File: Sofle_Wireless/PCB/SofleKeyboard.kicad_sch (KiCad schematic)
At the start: 139 parts, among them J1 Conn_01x05, J2 Conn_01x02, SW1 SW1, SW10 SW10, SW11 SW11, SW12 SW12, SW13 SW13, SW14 SW14, SW15 SW15, SW16 SW16, SW17 SW17, SW18 SW18, SW19 SW19, SW2 SW2, SW20 SW20, SW21 SW21, SW22 SW22, SW23 SW23, SW24 SW24, SW25 SW19, SW26 SW26, SW27 SW27, SW28 SW28, SW29 SW29, SW3 SW3, SW30 SW30, SW4 SW4, SW5 SW5, SW6 SW6, SW7 SW7, SW8 SW8, SW9 SW9, U1 NICE!NANO

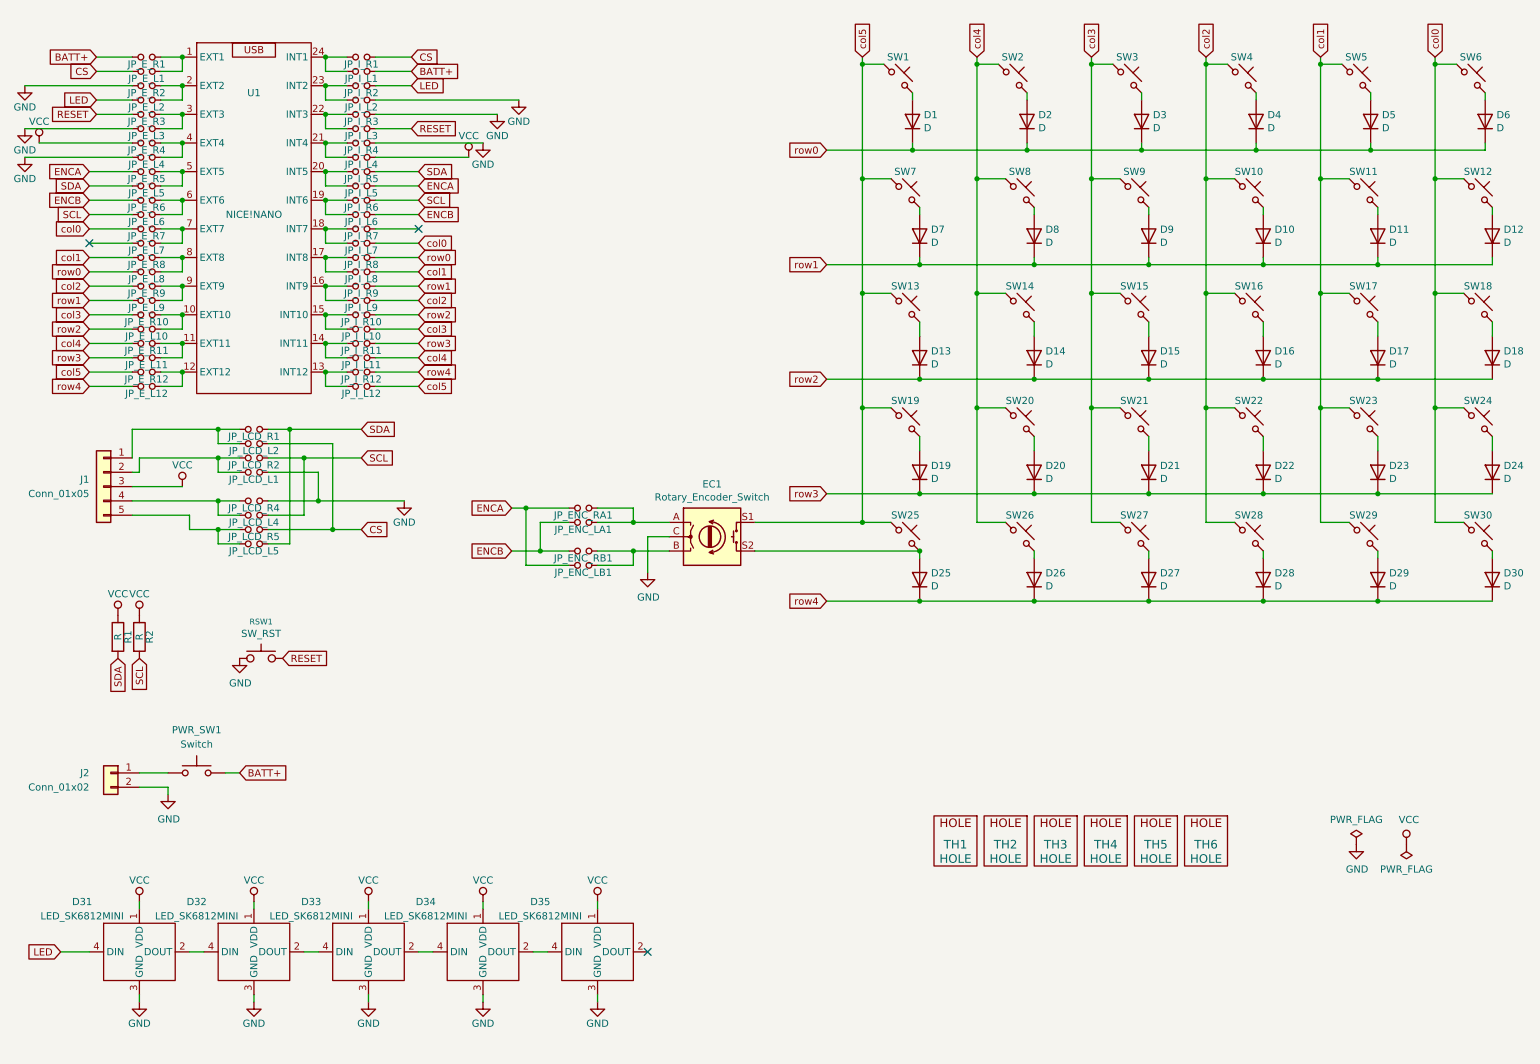
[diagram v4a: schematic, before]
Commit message: Exploration of multiple sheet for Schematic
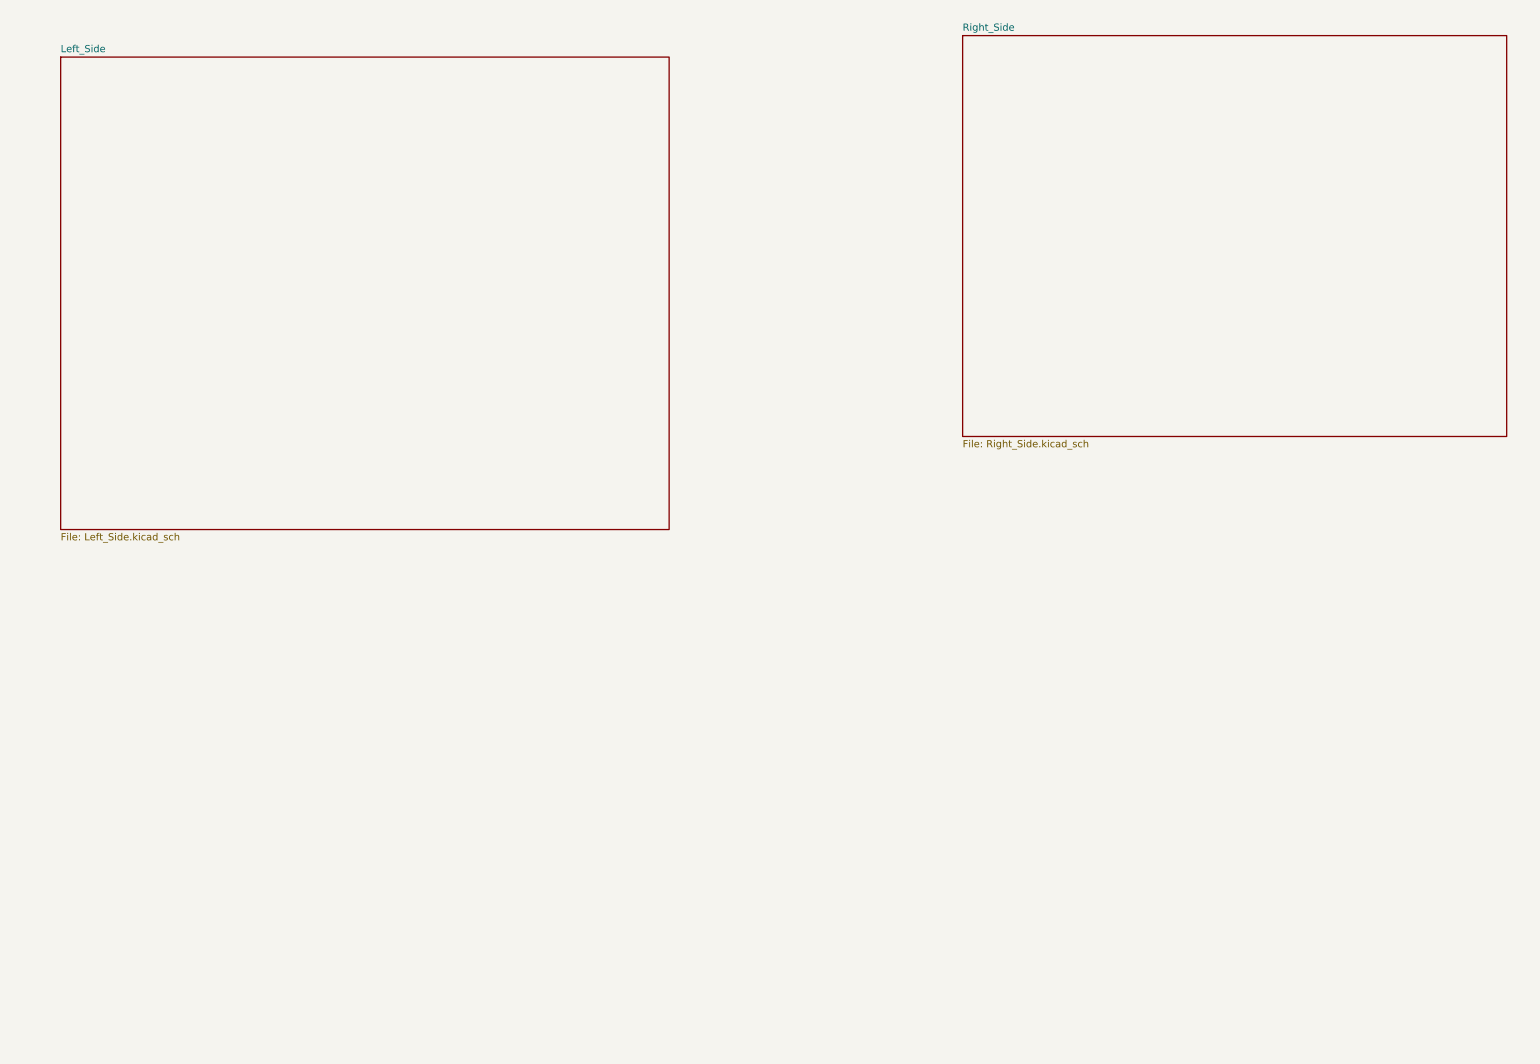
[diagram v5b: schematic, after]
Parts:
- removed D1, D10, D11, D12, D13, D14, D15, D16, D17, D18, D19, D2, D20, D21, D22, D23, D24, D25, D26, D27, D28, D29, D3, D30, D4, D5, D6, D7, D8, D9: D, Mechanical_Switches:Diode_SOD-123(dual side), symbol ScottoKeebs:Placeholder_Diode
- removed D31, D32, D33, D34, D35: LED_SK6812MINI, RGB_LED:SK6812_Mini-E_DualSide, symbol RGB_LED:SK6812_Mini-E
- removed EC1: Rotary_Encoder_Switch, Mechanical_Switches:RotaryEncoder_Alps_EC12E-Switch_Vertical_H20mm, symbol SofleKeyboard-rescue:Rotary_Encoder_Switch-Device
- removed J1: Conn_01x05, Mechanical_Switches:NICE!VIEW, symbol Connector_Generic:Conn_01x05
- removed J2: Conn_01x02, Mechanical_Switches:JST_PH_S2B-PH-SM4-TB_1x02-1MP_P2.00mm_Horizontal_DualSide, symbol Connector_Generic:Conn_01x02
- removed JP_ENC_LA1, JP_ENC_LB1, JP_E_L1, JP_E_L10, JP_E_L11, JP_E_L12, JP_E_L2, JP_E_L3, JP_E_L4, JP_E_L5, JP_E_L6, JP_E_L7, JP_E_L8, JP_E_L9, JP_LCD_L1, JP_LCD_L2, JP_LCD_L4, JP_LCD_L5: Jumper_NO_Small, Mechanical_Switches:SolderJumper-2_P1.3mm_Open_TrianglePad1.0x1.5mm_E, symbol SofleKeyboard-rescue:Jumper_NO_Small-Device
- removed JP_ENC_RA1, JP_ENC_RB1, JP_E_R1, JP_E_R10, JP_E_R11, JP_E_R12, JP_E_R2, JP_E_R3, JP_E_R4, JP_E_R5, JP_E_R6, JP_E_R7, JP_E_R8, JP_E_R9, JP_LCD_R1, JP_LCD_R2, JP_LCD_R4, JP_LCD_R5: Jumper_NO_Small, Mechanical_Switches:SolderJumper-2_P1.3mm_Open_TrianglePad1.0x1.5mm_E_Reverse, symbol SofleKeyboard-rescue:Jumper_NO_Small-Device
- removed JP_I_L1, JP_I_L10, JP_I_L11, JP_I_L12, JP_I_L2, JP_I_L3, JP_I_L4, JP_I_L5, JP_I_L6, JP_I_L7, JP_I_L8, JP_I_L9: Jumper_NO_Small, Mechanical_Switches:SolderJumper-2_P1.3mm_Open_TrianglePad1.0x1.5mm_I, symbol SofleKeyboard-rescue:Jumper_NO_Small-Device
- removed JP_I_R1, JP_I_R10, JP_I_R11, JP_I_R12, JP_I_R2, JP_I_R3, JP_I_R4, JP_I_R5, JP_I_R6, JP_I_R7, JP_I_R8, JP_I_R9: Jumper_NO_Small, Mechanical_Switches:SolderJumper-2_P1.3mm_Open_TrianglePad1.0x1.5mm_I_Reverse, symbol SofleKeyboard-rescue:Jumper_NO_Small-Device
- removed PWR_SW1: Switch, Mechanical_Switches:SLW-1276864-4A-D, symbol ScottoKeebs:Placeholder_Switch
- removed R1, R2: R, Mechanical_Switches:R_0805_2012Metric_Pad1.20x1.40mm_HandSolder_dualside, symbol SofleKeyboard-rescue:R-Lily58-cache-Lily58_Pro-rescue
- removed RSW1: SW_RST, Mechanical_Switches:ResetSW_DualSide, symbol SofleKeyboard-rescue:SW_RST-Lily58-cache-Lily58_Pro-rescue
- removed SW1: SW1, Mechanical_Switches:SW_MXHS_CHOCV1V2HS_1U, symbol ScottoKeebs:Placeholder_Keyswitch
- removed SW10: SW10, Mechanical_Switches:SW_MXHS_CHOCV1V2HS_1U, symbol ScottoKeebs:Placeholder_Keyswitch
- removed SW11: SW11, Mechanical_Switches:SW_MXHS_CHOCV1V2HS_1U, symbol ScottoKeebs:Placeholder_Keyswitch
- removed SW12: SW12, Mechanical_Switches:SW_MXHS_CHOCV1V2HS_1U, symbol ScottoKeebs:Placeholder_Keyswitch
- removed SW13: SW13, Mechanical_Switches:SW_MXHS_CHOCV1V2HS_1U, symbol ScottoKeebs:Placeholder_Keyswitch
- removed SW14: SW14, Mechanical_Switches:SW_MXHS_CHOCV1V2HS_1U, symbol ScottoKeebs:Placeholder_Keyswitch
- removed SW15: SW15, Mechanical_Switches:SW_MXHS_CHOCV1V2HS_1U, symbol ScottoKeebs:Placeholder_Keyswitch
- removed SW16: SW16, Mechanical_Switches:SW_MXHS_CHOCV1V2HS_1U, symbol ScottoKeebs:Placeholder_Keyswitch
- removed SW17: SW17, Mechanical_Switches:SW_MXHS_CHOCV1V2HS_1U, symbol ScottoKeebs:Placeholder_Keyswitch
- removed SW18: SW18, Mechanical_Switches:SW_MXHS_CHOCV1V2HS_1U, symbol ScottoKeebs:Placeholder_Keyswitch
- removed SW19, SW25: SW19, Mechanical_Switches:SW_MXHS_CHOCV1V2HS_1U, symbol ScottoKeebs:Placeholder_Keyswitch
- removed SW2: SW2, Mechanical_Switches:SW_MXHS_CHOCV1V2HS_1U, symbol ScottoKeebs:Placeholder_Keyswitch
- removed SW20: SW20, Mechanical_Switches:SW_MXHS_CHOCV1V2HS_1U, symbol ScottoKeebs:Placeholder_Keyswitch
- removed SW21: SW21, Mechanical_Switches:SW_MXHS_CHOCV1V2HS_1U, symbol ScottoKeebs:Placeholder_Keyswitch
- removed SW22: SW22, Mechanical_Switches:SW_MXHS_CHOCV1V2HS_1U, symbol ScottoKeebs:Placeholder_Keyswitch
- removed SW23: SW23, Mechanical_Switches:SW_MXHS_CHOCV1V2HS_1U, symbol ScottoKeebs:Placeholder_Keyswitch
- removed SW24: SW24, Mechanical_Switches:SW_MXHS_CHOCV1V2HS_1U, symbol ScottoKeebs:Placeholder_Keyswitch
- removed SW26: SW26, Mechanical_Switches:SW_MXHS_CHOCV1V2HS_1.5U, symbol ScottoKeebs:Placeholder_Keyswitch
- removed SW27: SW27, Mechanical_Switches:SW_MXHS_CHOCV1V2HS_1U, symbol ScottoKeebs:Placeholder_Keyswitch
- removed SW28: SW28, Mechanical_Switches:SW_MXHS_CHOCV1V2HS_1U, symbol ScottoKeebs:Placeholder_Keyswitch
- removed SW29: SW29, Mechanical_Switches:SW_MXHS_CHOCV1V2HS_1U, symbol ScottoKeebs:Placeholder_Keyswitch
- removed SW3: SW3, Mechanical_Switches:SW_MXHS_CHOCV1V2HS_1U, symbol ScottoKeebs:Placeholder_Keyswitch
- removed SW30: SW30, Mechanical_Switches:SW_MXHS_CHOCV1V2HS_1U, symbol ScottoKeebs:Placeholder_Keyswitch
- removed SW4: SW4, Mechanical_Switches:SW_MXHS_CHOCV1V2HS_1U, symbol ScottoKeebs:Placeholder_Keyswitch
- removed SW5: SW5, Mechanical_Switches:SW_MXHS_CHOCV1V2HS_1U, symbol ScottoKeebs:Placeholder_Keyswitch
- removed SW6: SW6, Mechanical_Switches:SW_MXHS_CHOCV1V2HS_1U, symbol ScottoKeebs:Placeholder_Keyswitch
- removed SW7: SW7, Mechanical_Switches:SW_MXHS_CHOCV1V2HS_1U, symbol ScottoKeebs:Placeholder_Keyswitch
- removed SW8: SW8, Mechanical_Switches:SW_MXHS_CHOCV1V2HS_1U, symbol ScottoKeebs:Placeholder_Keyswitch
- removed SW9: SW9, Mechanical_Switches:SW_MXHS_CHOCV1V2HS_1U, symbol ScottoKeebs:Placeholder_Keyswitch
- removed TH1, TH2, TH3, TH4, TH5, TH6: HOLE, MountingHole:MountingHole_2.2mm_M2, symbol SofleKeyboard-rescue:HOLE-Lily58-cache-Lily58_Pro-rescue
- removed U1: NICE!NANO, Mechanical_Switches:NICE!NANO, symbol Mechanical_Switches:Nice!Nano_V2(dual_use_socket)
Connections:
- no-connect marks 3 -> 0
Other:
- added sheet Left_Side (Left_Side.kicad_sch)
- added sheet Right_Side (Right_Side.kicad_sch)
